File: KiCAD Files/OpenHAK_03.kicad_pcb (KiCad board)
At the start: 4 copper layers, 38.1 x 25.4 mm, 52 parts, among them P1 Harwin M52 Series, P2 USB_OTG, U1 rfd_77101, U2 MAX30100, U3 MIC5365-1.8YMT-TZ, U4 BMI160, U5 MCP73831T-2ATI/OT, U6 MIC5365-3.0YMT-TZ, U7 TXS0102DQER

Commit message: Added PDFs of the top and bottom
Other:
- board text added: "BIOHACKING VILLAGE"
- board text removed: "BIOHACK VILLAGE"
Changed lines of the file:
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@@
       (xy -3.228344 8.4504)) (layer B.SilkS) (width 0.01))
   )
-  (gr_text "BIOHACK\nVILLAGE" (at 132.04 106.16) (layer F.SilkS)
-    (effects (font (size 1 1) (thickness 0.2) italic) (justify left))
+  (gr_text "BIOHACKING\nVILLAGE" (at 138.12 106.36) (layer F.SilkS)
+    (effects (font (size 1 1) (thickness 0.2) italic) (justify right))
   )
   (gr_text DEFCON27 (at 131.3 99.62 90) (layer B.SilkS)
@@
     (effects (font (size 1 1) (thickness 0.25)) (justify mirror))
   )
-  (gr_text DEFCON27 (at 132.44088 108.99386) (layer F.SilkS)
+  (gr_text DEFCON27 (at 132.61 109.2) (layer F.SilkS)
     (effects (font (size 1.5 1.5) (thickness 0.3) italic))
   )

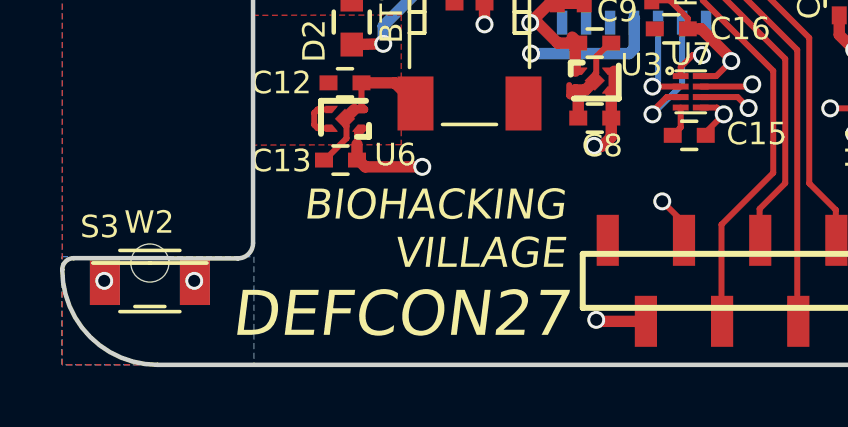
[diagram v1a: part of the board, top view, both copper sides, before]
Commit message: adjusted pad to mask clearance for DFM
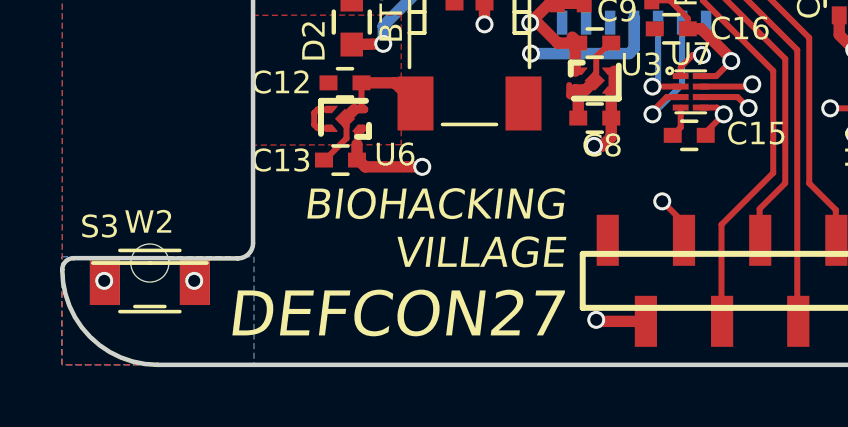
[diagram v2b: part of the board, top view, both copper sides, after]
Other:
- rule pad_to_mask_clearance: 0.03 -> 0.02
- rule solder_mask_min_width: 0.25 -> 0.05
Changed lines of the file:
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@@
     (pad_size 1.2 1.8)
     (pad_drill 0)
-    (pad_to_mask_clearance 0.03)
-    (solder_mask_min_width 0.25)
+    (pad_to_mask_clearance 0.02)
+    (solder_mask_min_width 0.05)
     (aux_axis_origin 121.34088 110.89386)
     (visible_elements FFFDFFFF)
@@
       (plotinvisibletext false)
       (padsonsilk false)
-      (subtractmaskfromsilk false)
+      (subtractmaskfromsilk true)
       (outputformat 1)
       (mirror false)
@@
     (add_net VDD)
   )
+  (module Solutions:X2SON8_1.4mm_x_1mm (layer F.Cu)
+    (at 142.29088 101.79386 270)
+    (solder_mask_margin 0.02)
+    (solder_paste_margin -0.02)
+    (attr smd)
+    (fp_text reference U7 (at -1.25 0) (layer F.SilkS)
+      (effects (font (size 0.75 0.75) (thickness 0.15)))
+    )
+    (fp_text value TXS0102DQER (at -0.35 -6.995 270) (layer F.Fab)
+      (effects (font (size 0.75 0.75) (thickness 0.15)))
+    )
+    (fp_line (start -0.7 -0.5) (end -0.7 0.5) (layer F.SilkS) (width 0.1))
+    (fp_line (start 0.7 -0.5) (end 0.7 0.5) (layer F.SilkS) (width 0.1))
+    (fp_circle (center -0.7 0.7) (end -0.6 0.7) (layer F.SilkS) (width 0.1))
+    (pad 1 smd rect (at -0.525 0.335 270) (size 0.2 0.53) (layers F.Cu F.Mask)
+      (net 46 +1V8) (solder_mask_margin 0.02) (solder_paste_margin -0.02) (clearance 0.1))
+    (pad 2 smd rect (at -0.175 0.335 270) (size 0.2 0.53) (layers F.Cu F.Mask)
+      (net 51 /1V8_SDA) (solder_mask_margin 0.02) (solder_paste_margin -0.02) (clearance 0.1))
+    (pad 3 smd rect (at 0.175 0.335 270) (size 0.2 0.53) (layers F.Cu F.Mask)
+      (net 49 /1V8_SCL) (solder_mask_margin 0.02) (solder_paste_margin -0.02) (clearance 0.1))
+    (pad 4 smd rect (at 0.525 0.335 270) (size 0.2 0.53) (layers F.Cu F.Mask)
+      (net 1 GND) (solder_mask_margin 0.02) (solder_paste_margin -0.02) (clearance 0.1))
+    (pad 5 smd rect (at 0.525 -0.335 270) (size 0.2 0.53) (layers F.Cu F.Mask)
+      (net 46 +1V8) (solder_mask_margin 0.02) (solder_paste_margin -0.02) (clearance 0.1))
+    (pad 6 smd rect (at 0.175 -0.335 270) (size 0.2 0.53) (layers F.Cu F.Mask)
+      (net 50 /3V3_SCL) (solder_mask_margin 0.02) (solder_paste_margin -0.02) (clearance 0.1))
+    (pad 7 smd rect (at -0.175 -0.335 270) (size 0.2 0.53) (layers F.Cu F.Mask)
+      (net 52 /3V3_SDA) (solder_mask_margin 0.02) (solder_paste_margin -0.02) (clearance 0.1))
+    (pad 8 smd rect (at -0.525 -0.335 270) (size 0.2 0.53) (layers F.Cu F.Mask)
+      (net 2 VDD) (solder_mask_margin 0.02) (solder_paste_margin -0.02) (clearance 0.1))
+    (pad "" smd rect (at -0.525 0.335 270) (size 0.165 0.53) (layers F.Paste))
+    (pad "" smd rect (at -0.175 0.335 270) (size 0.165 0.53) (layers F.Paste))
+    (pad "" smd rect (at 0.525 -0.335 270) (size 0.165 0.53) (layers F.Paste))
+    (pad "" smd rect (at 0.525 0.335 270) (size 0.165 0.53) (layers F.Paste))
+    (pad "" smd rect (at 0.175 0.335 270) (size 0.165 0.53) (layers F.Paste))
+    (pad "" smd rect (at 0.175 -0.335 270) (size 0.165 0.53) (layers F.Paste))
+    (pad "" smd rect (at -0.175 -0.335 270) (size 0.165 0.53) (layers F.Paste))
+    (pad "" smd rect (at -0.525 -0.335 270) (size 0.165 0.53) (layers F.Paste))
+  )
   (module Capacitors_SMD:C_0402 (layer F.Cu)
     (at 137.84088 98.29386 90)
@@
     (pad 5 smd rect (at 0 0 135) (size 0.48 0.48) (layers F.Cu F.Paste F.Mask)
       (net 1 GND))
-  )
-  (module Solutions:X2SON8_1.4mm_x_1mm (layer F.Cu)
-    (at 142.29088 101.79386 270)
-    (attr smd)
-    (fp_text reference U7 (at -1.25 0) (layer F.SilkS)
-      (effects (font (size 0.75 0.75) (thickness 0.15)))
-    )
-    (fp_text value TXS0102DQER (at -0.35 -6.995 270) (layer F.Fab)
-      (effects (font (size 0.75 0.75) (thickness 0.15)))
-    )
-    (fp_circle (center -0.7 0.7) (end -0.6 0.7) (layer F.SilkS) (width 0.1))
-    (fp_line (start 0.7 -0.5) (end 0.7 0.5) (layer F.SilkS) (width 0.1))
-    (fp_line (start -0.7 -0.5) (end -0.7 0.5) (layer F.SilkS) (width 0.1))
-    (pad "" smd rect (at -0.525 -0.335 270) (size 0.165 0.53) (layers F.Paste))
-    (pad "" smd rect (at -0.175 -0.335 270) (size 0.165 0.53) (layers F.Paste))
-    (pad "" smd rect (at 0.175 -0.335 270) (size 0.165 0.53) (layers F.Paste))
-    (pad "" smd rect (at 0.175 0.335 270) (size 0.165 0.53) (layers F.Paste))
-    (pad "" smd rect (at 0.525 0.335 270) (size 0.165 0.53) (layers F.Paste))
-    (pad "" smd rect (at 0.525 -0.335 270) (size 0.165 0.53) (layers F.Paste))
-    (pad "" smd rect (at -0.175 0.335 270) (size 0.165 0.53) (layers F.Paste))
-    (pad "" smd rect (at -0.525 0.335 270) (size 0.165 0.53) (layers F.Paste))
-    (pad 8 smd rect (at -0.525 -0.335 270) (size 0.2 0.53) (layers F.Cu F.Mask)
-      (net 2 VDD) (solder_mask_margin 0.05) (solder_paste_margin -0.035) (clearance 0.1))
-    (pad 7 smd rect (at -0.175 -0.335 270) (size 0.2 0.53) (layers F.Cu F.Mask)
-      (net 52 /3V3_SDA) (solder_mask_margin 0.05) (solder_paste_margin -0.035) (clearance 0.1))
-    (pad 6 smd rect (at 0.175 -0.335 270) (size 0.2 0.53) (layers F.Cu F.Mask)
-      (net 50 /3V3_SCL) (solder_mask_margin 0.05) (solder_paste_margin -0.035) (clearance 0.1))
-    (pad 5 smd rect (at 0.525 -0.335 270) (size 0.2 0.53) (layers F.Cu F.Mask)
-      (net 46 +1V8) (solder_mask_margin 0.05) (solder_paste_margin -0.035) (clearance 0.1))
-    (pad 4 smd rect (at 0.525 0.335 270) (size 0.2 0.53) (layers F.Cu F.Mask)
-      (net 1 GND) (solder_mask_margin 0.05) (solder_paste_margin -0.035) (clearance 0.1))
-    (pad 3 smd rect (at 0.175 0.335 270) (size 0.2 0.53) (layers F.Cu F.Mask)
-      (net 49 /1V8_SCL) (solder_mask_margin 0.05) (solder_paste_margin -0.035) (clearance 0.1))
-    (pad 2 smd rect (at -0.175 0.335 270) (size 0.2 0.53) (layers F.Cu F.Mask)
-      (net 51 /1V8_SDA) (solder_mask_margin 0.05) (solder_paste_margin -0.035) (clearance 0.1))
-    (pad 1 smd rect (at -0.525 0.335 270) (size 0.2 0.53) (layers F.Cu F.Mask)
-      (net 46 +1V8) (solder_mask_margin 0.05) (clearance 0.1))
   )
   (module Solutions:MAX30100 (layer B.Cu)
@@
     (effects (font (size 1 1) (thickness 0.25)) (justify mirror))
   )
-  (gr_text DEFCON27 (at 132.61 109.2) (layer F.SilkS)
+  (gr_text DEFCON27 (at 132.45 109.22) (layer F.SilkS)
     (effects (font (size 1.5 1.5) (thickness 0.3) italic))
   )
